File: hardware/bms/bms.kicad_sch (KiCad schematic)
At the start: 23 parts

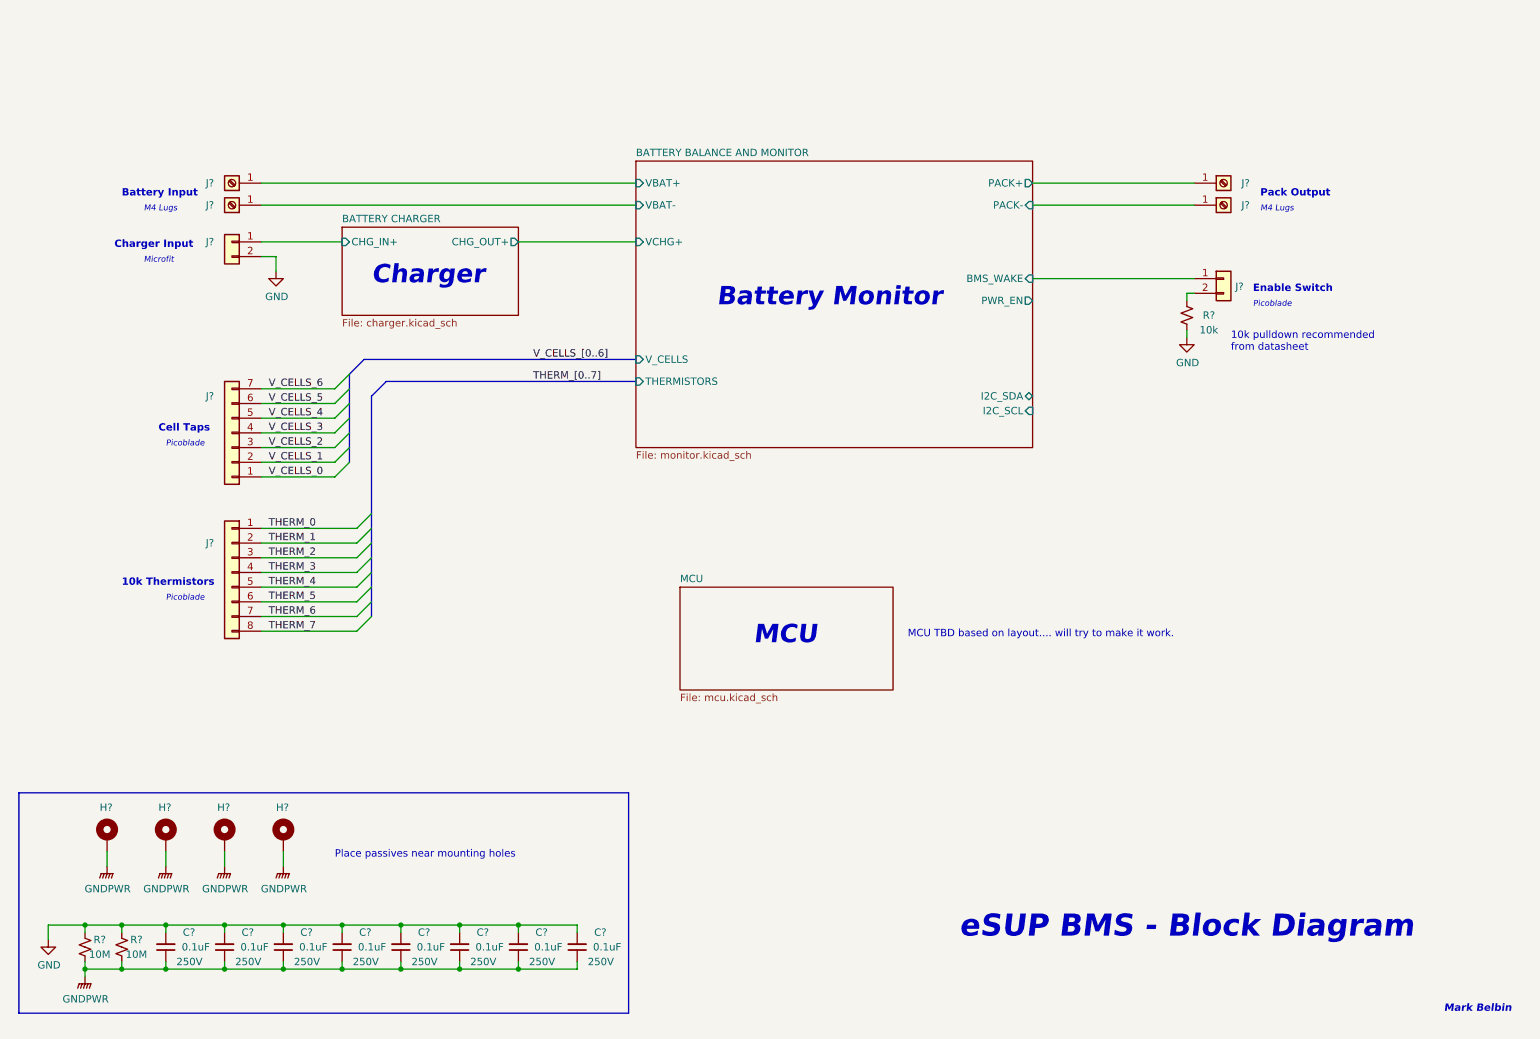
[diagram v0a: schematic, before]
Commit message: Added charger and pack fuses directly to board
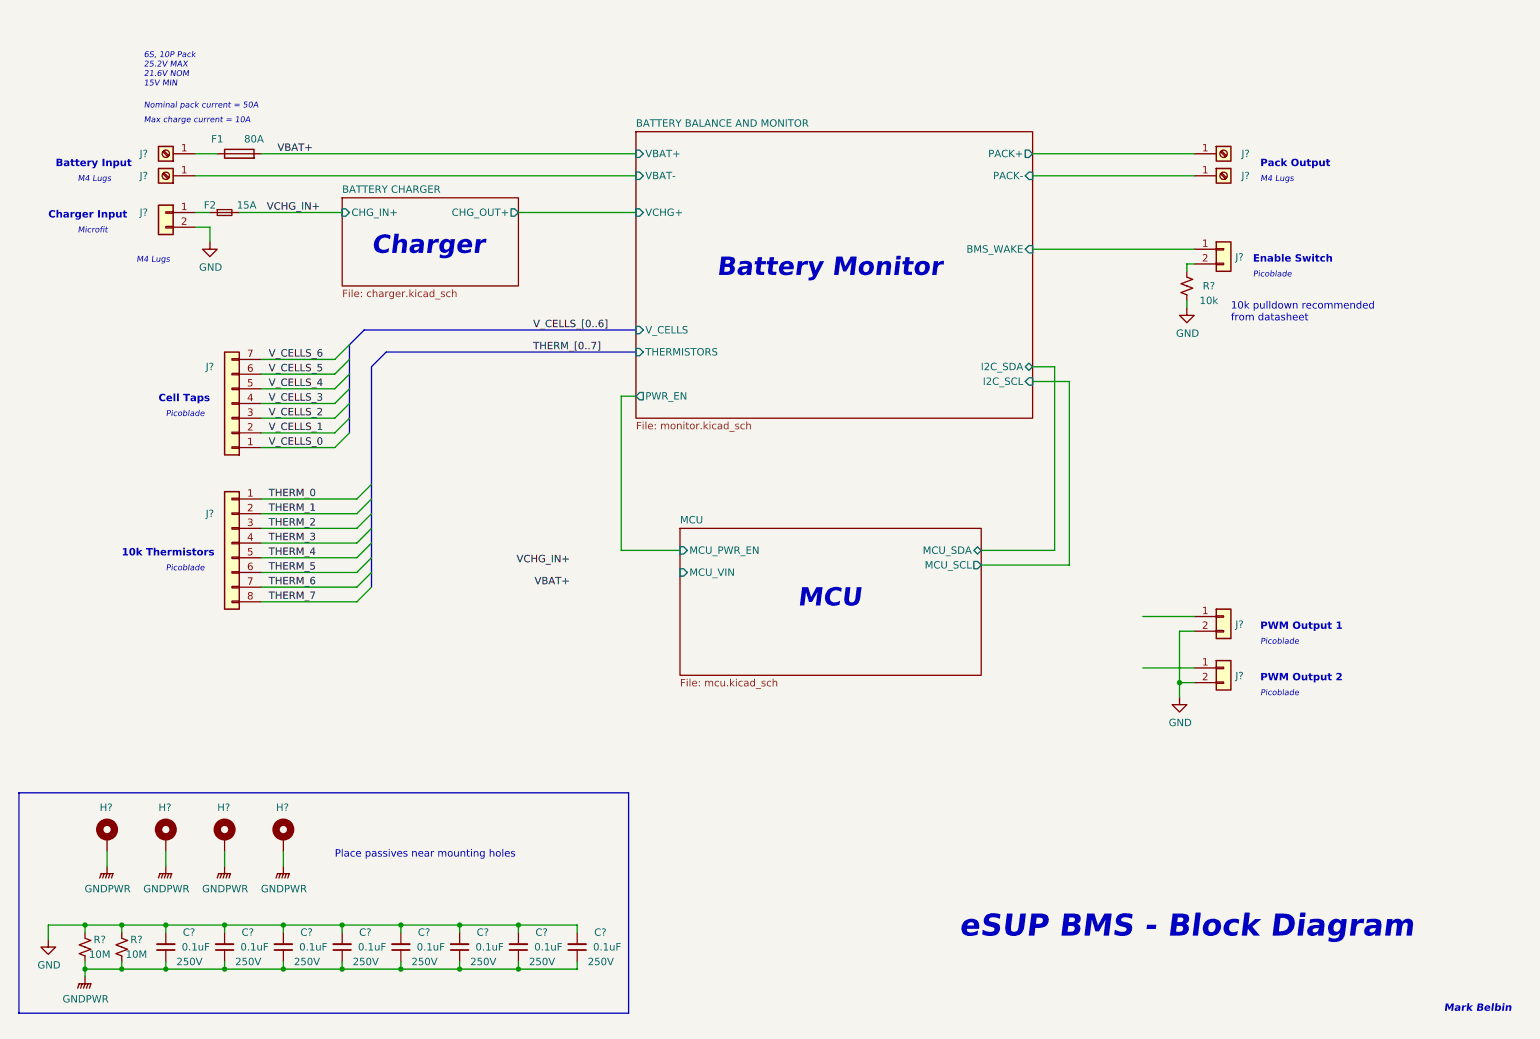
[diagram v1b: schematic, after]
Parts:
- added F1: 80A, bms:FUSE_0ACH-9800-TE_BEL, symbol Device:Fuse
- added F2: 15A, bms:FUSC6125X279N, symbol Device:Fuse_Small
- added J? (x2): Conn_01x02, Connector_Molex:Molex_PicoBlade_53261-0271_1x02-1MP_P1.25mm_Horizontal, symbol Connector_Generic:Conn_01x02
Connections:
- net GND: now also J?.2 (Pin_2), J?.2 (Pin_2)
- net BATTERY BALANCE AND MONITOR/VBAT+: no longer names the net of J?.1 (Pin_1)
- net BATTERY BALANCE AND MONITOR/VBAT+: now also F1.1
- net BATTERY CHARGER/CHG_IN+: no longer names the net of J?.1 (Pin_1)
- net BATTERY CHARGER/CHG_IN+: now also F2.1
- new net VBAT+: F1.2
- new net VCHG_IN+: F2.2
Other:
- sheet MCU ports: added MCU_PWR_EN, MCU_SCL, MCU_SDA, MCU_VIN; removed none
- note added: "6S, 10P Pack 25.2V MAX 21.6V NOM 15V MIN"
- note added: "Max charge current = 10A"
- note added: "Nominal pack current = 50A"
- note added: "PWM Output 1"
- note added: "PWM Output 2"
- note removed: "MCU TBD based on layout.... will try to make it work."
- moved on the sheet: J?, R?

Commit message: More charger sch progress
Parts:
- added D1: SMAJ28A, Diode_SMD:D_SMA, symbol Diode:SMAJ28A
- added J?: USB_C_Plug_USB2.0, symbol Connector:USB_C_Plug_USB2.0
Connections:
- net GND: now also D1.2 (A2)
- net VCHG_IN+: no longer F2.2
- net VCHG_IN: now reaches F2.1, J?.1 (Pin_1)
- net VCHG_IN: now also D1.1 (A1)
- net VBAT_IN: now reaches F1.1, J?.1 (Pin_1)
- net MCU/PWM_OUT1: now reaches J?.1 (Pin_1)
- net MCU/PWM_OUT2: now reaches J?.1 (Pin_1)
- new net: J?.A1 (GND), J?.A12 (GND), J?.B1 (GND), J?.B12 (GND)
- new net: J?.A4 (VBUS), J?.A9 (VBUS), J?.B4 (VBUS), J?.B9 (VBUS)
- new net VCHG_IN_F: F2.2
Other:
- sheet MCU ports: added PWM_OUT1, PWM_OUT2; removed none
- moved on the sheet: F1, F2, J?, R?

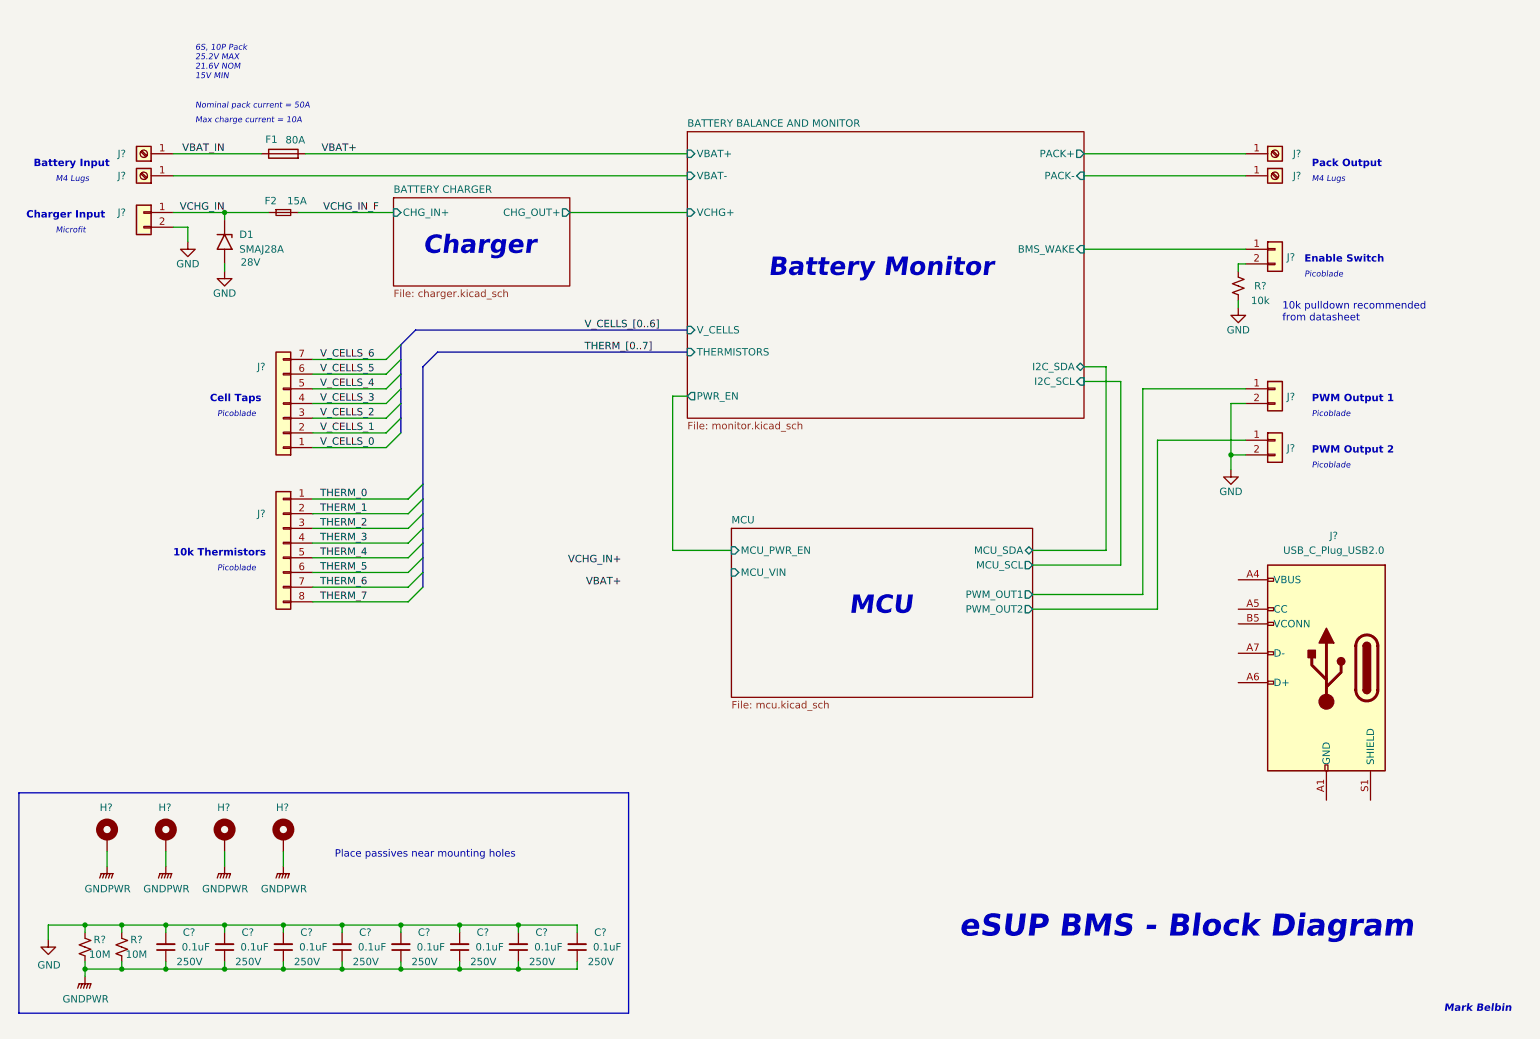
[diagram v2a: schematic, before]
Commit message: Added another thermistor for charger temp sensings. 9 total for the whole pack now
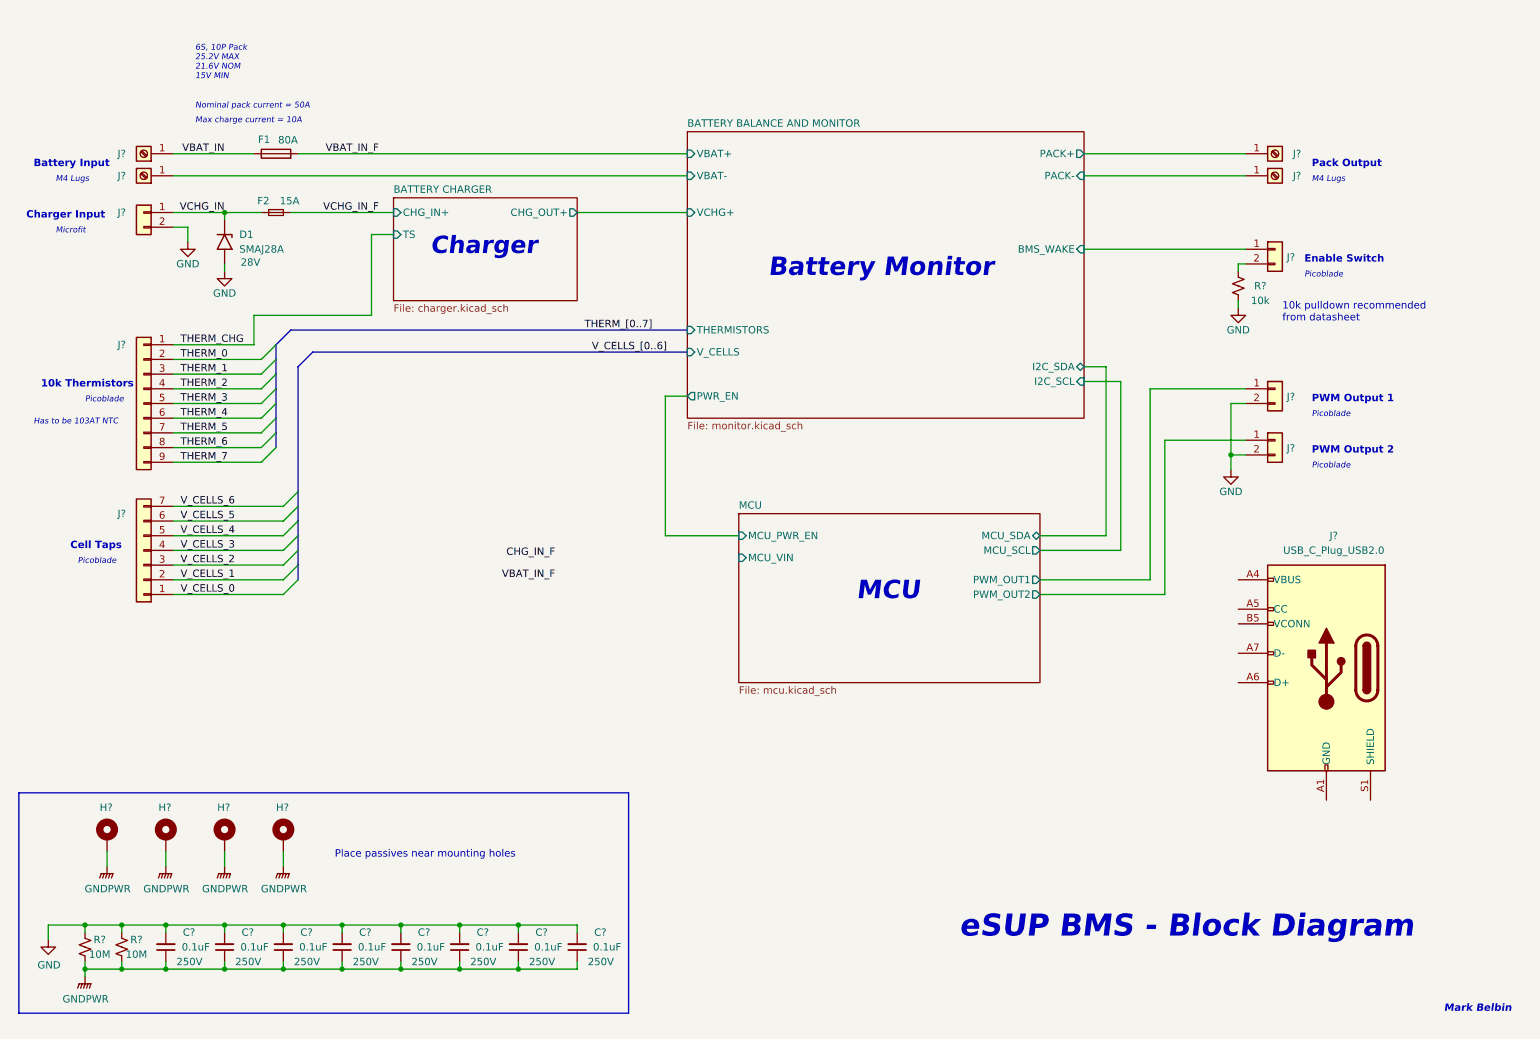
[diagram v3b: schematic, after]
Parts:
- removed J?: Conn_01x08, Connector_Molex:Molex_PicoBlade_53261-0871_1x08-1MP_P1.25mm_Horizontal, symbol Connector_Generic:Conn_01x08
- added J?: Conn_01x09, symbol Connector_Generic:Conn_01x09
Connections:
- net THERM_0: now also J?.2 (Pin_2)
- net THERM_1: now also J?.3 (Pin_3)
- net THERM_2: now also J?.4 (Pin_4)
- net THERM_3: now also J?.5 (Pin_5)
- net THERM_4: now also J?.6 (Pin_6)
- net THERM_5: now also J?.7 (Pin_7)
- net THERM_6: now also J?.8 (Pin_8)
- net THERM_7: now also J?.9 (Pin_9)
- net VBAT+ renamed VBAT_IN_F
- new net THERM_CHG: J?.1 (Pin_1)
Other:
- sheet BATTERY CHARGER ports: added TS; removed none
- note added: "Has to be 103AT NTC"
- moved on the sheet: F1, F2, J?

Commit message: Made more progress on charger sch. Need to complete power stage next. Also added diode OR for MCU power conv input. Still deciding on converter selection
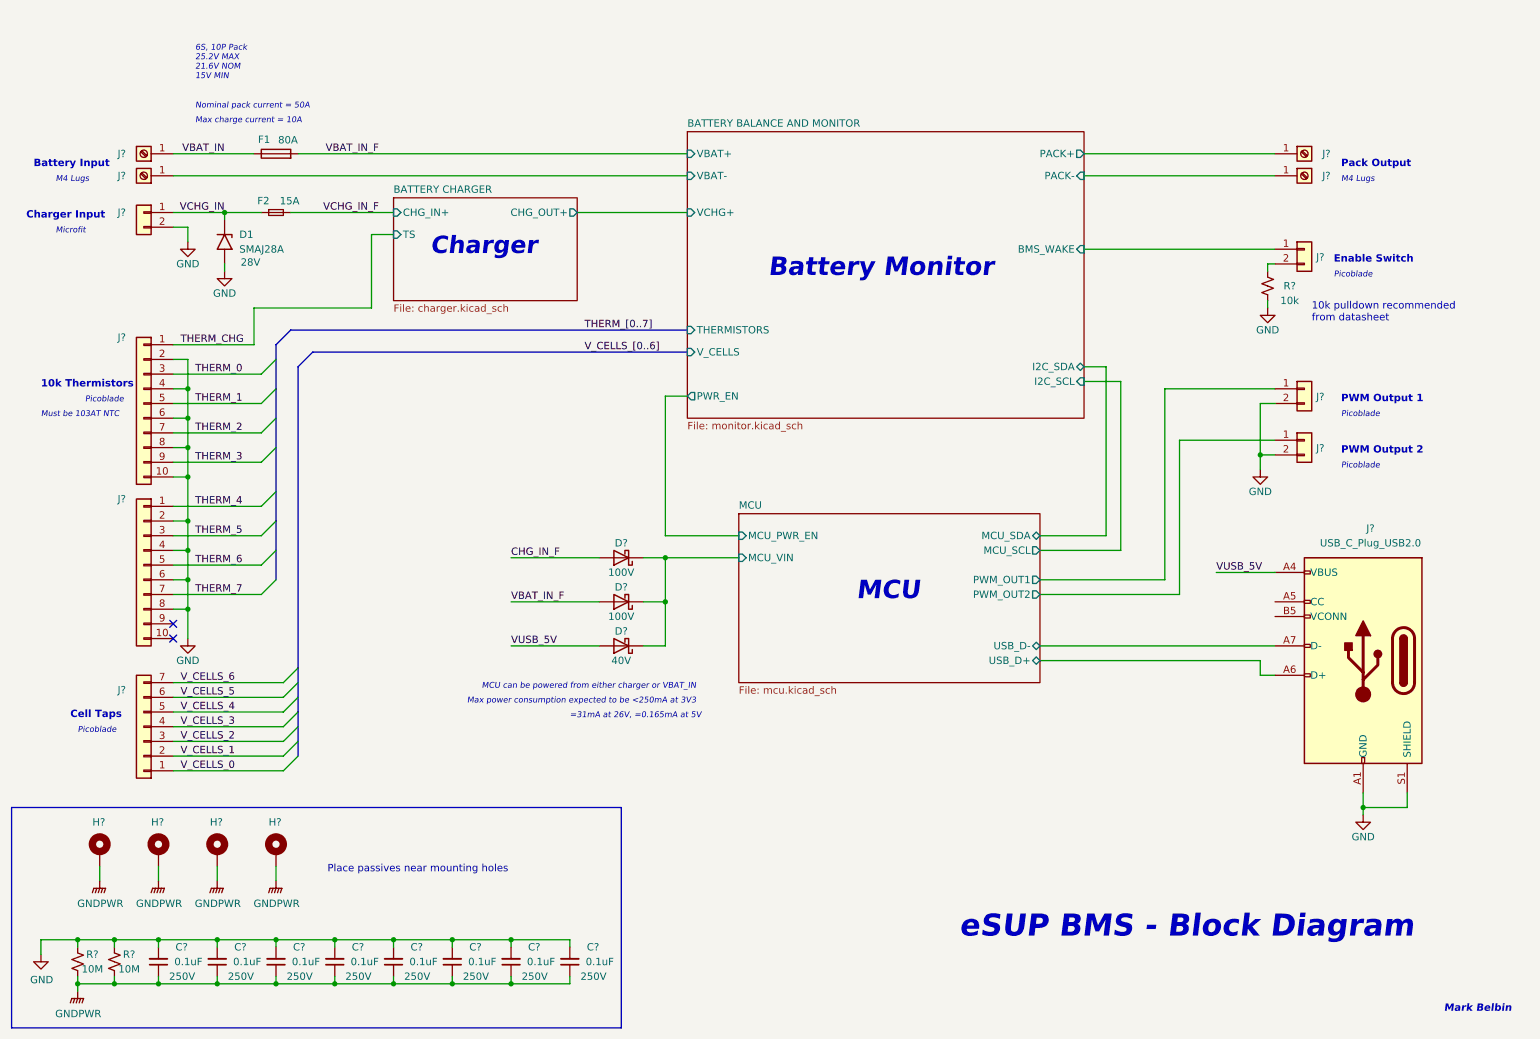
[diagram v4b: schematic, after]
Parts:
- removed J?: Conn_01x09, symbol Connector_Generic:Conn_01x09
- added D?: D_Schottky, Diode_SMD:D_SOD-123, symbol Device:D_Schottky
- added D? (x2): D_Schottky, Diode_SMD:D_SOD-123F, symbol Device:D_Schottky
- added J? (x2): Conn_01x10, Connector_Molex:Molex_PicoBlade_53261-1071_1x10-1MP_P1.25mm_Horizontal, symbol Connector_Generic:Conn_01x10
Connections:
- net CHG_IN_F: now also D?.2 (A)
- net GND: now also J?.A1 (GND), J?.A12 (GND), J?.B1 (GND), J?.B12 (GND), J?.S1 (SHIELD), J?.10 (Pin_10), J?.2 (Pin_2), J?.2 (Pin_2), J?.4 (Pin_4), J?.4 (Pin_4), J?.6 (Pin_6), J?.6 (Pin_6), J?.8 (Pin_8), J?.8 (Pin_8)
- net MCU/MCU_VIN: now also D?.1 (K), D?.1 (K), D?.1 (K)
- net THERM_0: now also J?.3 (Pin_3)
- net THERM_1: now also J?.5 (Pin_5)
- net THERM_2: now also J?.7 (Pin_7)
- net THERM_3: now also J?.9 (Pin_9)
- net THERM_4: now also J?.1 (Pin_1)
- net THERM_5: now also J?.3 (Pin_3)
- net THERM_6: now also J?.5 (Pin_5)
- net THERM_7: now also J?.7 (Pin_7)
- net THERM_CHG: now also J?.1 (Pin_1)
- net VBAT_IN_F: now also D?.2 (A)
- net VUSB_5V: now reaches J?.A4 (VBUS), J?.A9 (VBUS), J?.B4 (VBUS), J?.B9 (VBUS)
- net VUSB_5V: now also D?.2 (A)
- net MCU/USB_D+: now reaches J?.A6 (D+)
- net MCU/USB_D-: now reaches J?.A7 (D-)
- no-connect marks 0 -> 2
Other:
- sheet MCU ports: added USB_D+, USB_D-; removed none
- note added: "=31mA at 26V, =0.165mA at 5V"
- note added: "MCU can be powered from either charger or VBAT_IN"
- note added: "Max power consumption expected to be <250mA at 3V3"
- note added: "Must be 103AT NTC"
- note removed: "Has to be 103AT NTC"
- moved on the sheet: C?, H?, J?, R?
